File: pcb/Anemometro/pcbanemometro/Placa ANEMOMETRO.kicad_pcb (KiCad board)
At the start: 2 copper layers, 35.2 x 30 mm, 14 parts, among them J1 Conn_01x03, J2 Conn_01x03, U1 TL082

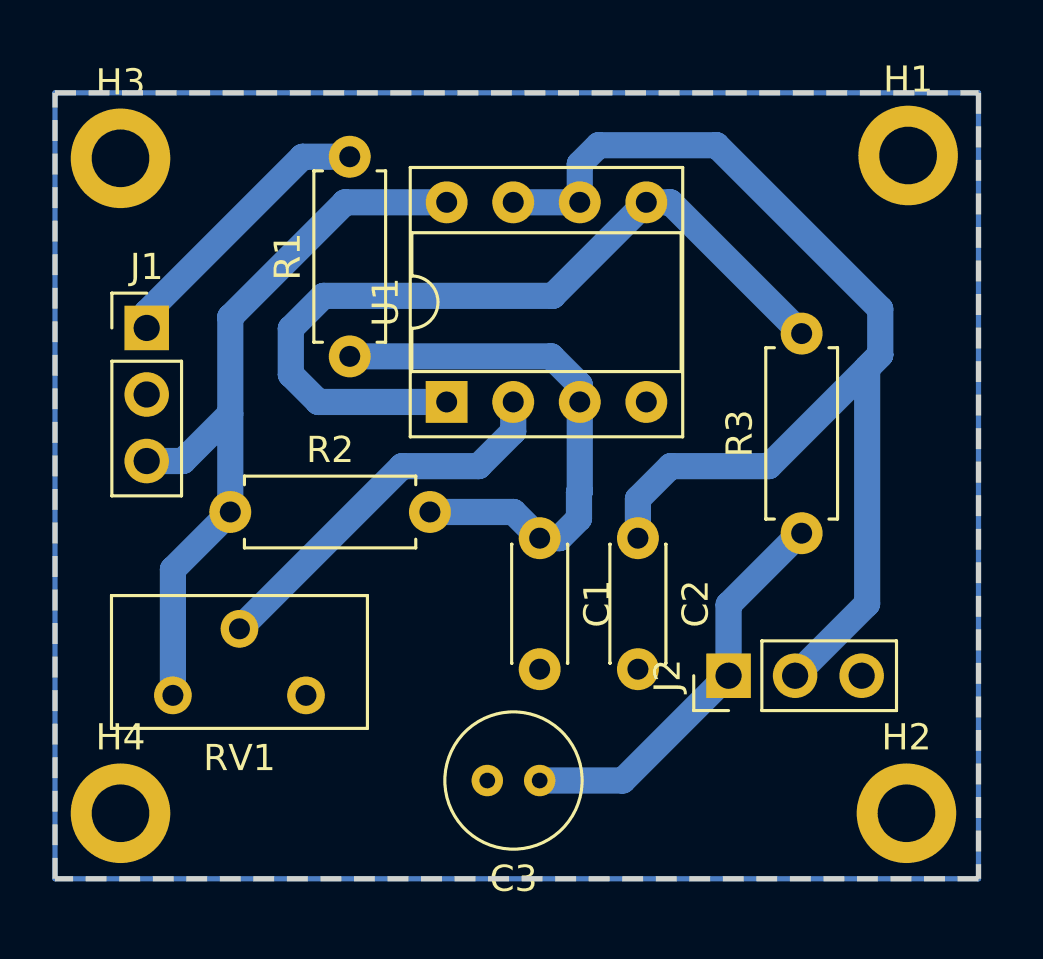
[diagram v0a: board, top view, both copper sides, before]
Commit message: se readaptaron y revisaron las PCBs, listas para imprimir
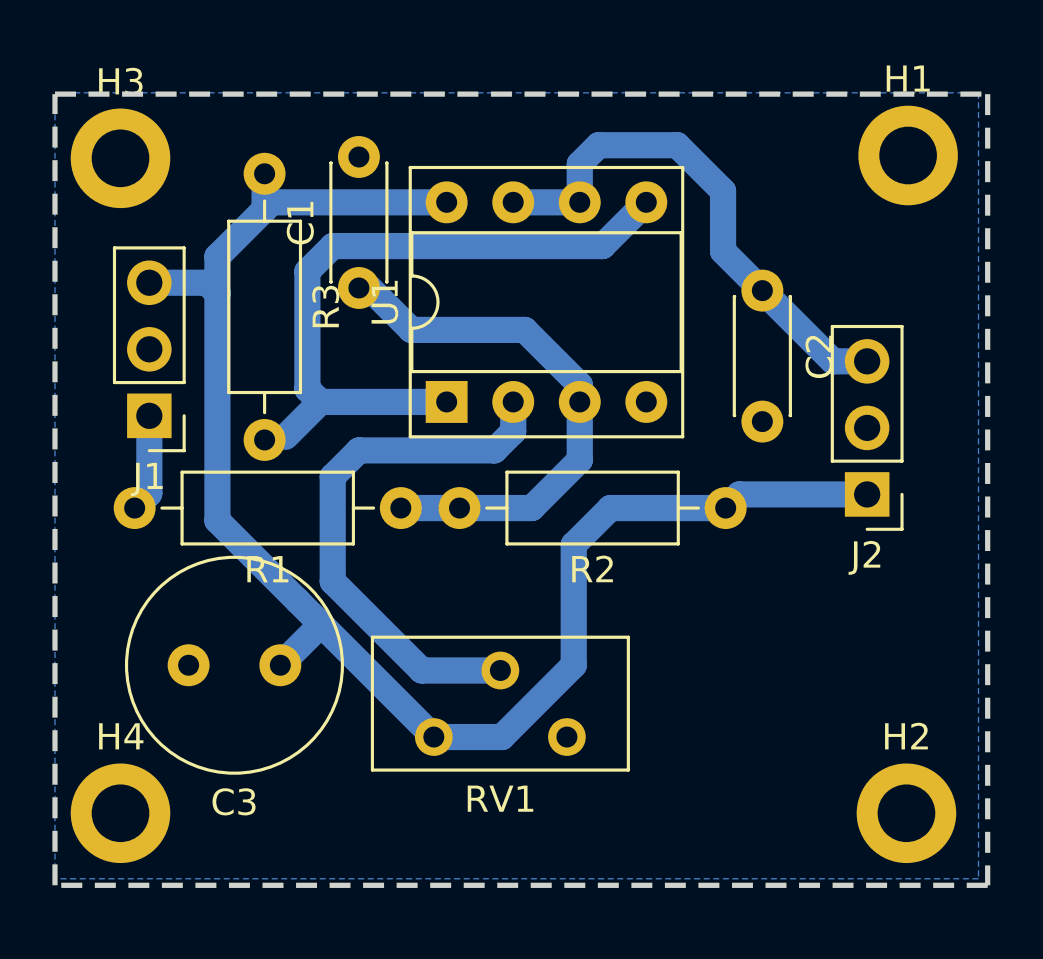
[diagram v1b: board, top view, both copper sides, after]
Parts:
- C3: footprint Capacitor_THT:C_Radial_D5.0mm_H7.0mm_P2.00mm -> Capacitor_THT:C_Radial_D8.0mm_H7.0mm_P3.50mm
- J2: value Conn_01x03 -> ToMother
- R1, R2, R3: footprint Resistor_THT:R_Axial_DIN0207_L6.3mm_D2.5mm_P7.62mm_Horizontal -> Resistor_THT:R_Axial_DIN0207_L6.3mm_D2.5mm_P10.16mm_Horizontal
- moved R3 24.7 mm to (83.0, 27.8), turned to -90 degrees
- moved R2 18.9 mm to (100.6, 40.6), turned to 180 degrees
- moved C1 11.8 mm to (86.6, 32.2), turned to 90 degrees
- moved C3 10.8 mm to (83.6, 46.6)
- moved C2 10.6 mm to (102.0, 32.3)
- moved RV1 10.1 mm to (89.5, 49.3)
- moved J2 8.71 mm to (106.0, 40.1), turned to 180 degrees
- moved R1 6.11 mm to (88.2, 40.6), turned to 180 degrees
- moved J1 3.36 mm to (78.6, 37.1), turned to 180 degrees
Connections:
- J2 pad 2: D_hall -> GND_G1
- J2 pad 3: GND_G1 -> D_hall
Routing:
- net D_hall: track 46.7 -> 20.0 mm
- net 3.3V: track 44.9 -> 60.8 mm
- net Net-(J1-Pin_1): track 10.8 -> 3.75 mm
- net Net-(U1A--): track 14.7 -> 20.5 mm
- net Net-(U1B-+): track 31.8 -> 26.0 mm
- net Net-(U1A-+): track 20.8 -> 20.0 mm
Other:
- board size 35.2 x 30 mm -> 35.6 x 30.2 mm

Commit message: Se agregó la modificación del MQ135 a 5v con divisor resistivo; además de cambio del DHT del pin 12; también se modificaron los pines de conexión
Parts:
- added C1: 104, Capacitor_THT:C_Disc_D4.3mm_W1.9mm_P5.00mm, F.Cu at (151.4, 121.8)
- added C1: 104, Capacitor_THT:C_Disc_D4.3mm_W1.9mm_P5.00mm, F.Cu at (205.2, 120.8)
- added C1: 104, Capacitor_THT:C_Disc_D4.3mm_W1.9mm_P5.00mm, F.Cu at (96.2, 123.0)
- added C1: 104, Capacitor_THT:C_Disc_D4.3mm_W1.9mm_P5.00mm, F.Cu at (205.4, 76.2)
- added C1: 104, Capacitor_THT:C_Disc_D4.3mm_W1.9mm_P5.00mm, F.Cu at (152.0, 77.4)
- added C2: 104, Capacitor_THT:C_Disc_D4.3mm_W1.9mm_P5.00mm, F.Cu at (220.6, 120.9)
- added C2: 104, Capacitor_THT:C_Disc_D4.3mm_W1.9mm_P5.00mm, F.Cu at (167.4, 77.5)
- added C2: 104, Capacitor_THT:C_Disc_D4.3mm_W1.9mm_P5.00mm, F.Cu at (111.6, 123.2)
- added C2: 104, Capacitor_THT:C_Disc_D4.3mm_W1.9mm_P5.00mm, F.Cu at (166.8, 121.9)
- added C2: 104, Capacitor_THT:C_Disc_D4.3mm_W1.9mm_P5.00mm, F.Cu at (220.8, 76.3)
- added C3: 220uF, Capacitor_THT:C_Radial_D8.0mm_H7.0mm_P3.50mm, F.Cu at (93.2, 137.4)
- added C3: 220uF, Capacitor_THT:C_Radial_D8.0mm_H7.0mm_P3.50mm, F.Cu at (202.4, 90.6)
- added C3: 220uF, Capacitor_THT:C_Radial_D8.0mm_H7.0mm_P3.50mm, F.Cu at (148.4, 136.2)
- added C3: 220uF, Capacitor_THT:C_Radial_D8.0mm_H7.0mm_P3.50mm, F.Cu at (149.0, 91.8)
- added C3: 220uF, Capacitor_THT:C_Radial_D8.0mm_H7.0mm_P3.50mm, F.Cu at (202.2, 135.2)
- added H1: MountingHole_Pad, MountingHole:MountingHole_2.2mm_M2_DIN965_Pad, F.Cu at (226.2, 115.7)
- added H1: MountingHole_Pad, MountingHole:MountingHole_2.2mm_M2_DIN965_Pad, F.Cu at (172.4, 116.7)
- added H1: MountingHole_Pad, MountingHole:MountingHole_2.2mm_M2_DIN965_Pad, F.Cu at (117.2, 118.0)
- added H1: MountingHole_Pad, MountingHole:MountingHole_2.2mm_M2_DIN965_Pad, F.Cu at (226.4, 71.1)
- added H1: MountingHole_Pad, MountingHole:MountingHole_2.2mm_M2_DIN965_Pad, F.Cu at (173.0, 72.3)
- added H2: MountingHole_Pad, MountingHole:MountingHole_2.2mm_M2_DIN965_Pad, F.Cu at (117.1, 143.1)
- added H2: MountingHole_Pad, MountingHole:MountingHole_2.2mm_M2_DIN965_Pad, F.Cu at (172.3, 141.8)
- added H2: MountingHole_Pad, MountingHole:MountingHole_2.2mm_M2_DIN965_Pad, F.Cu at (226.3, 96.2)
- added H2: MountingHole_Pad, MountingHole:MountingHole_2.2mm_M2_DIN965_Pad, F.Cu at (226.1, 140.8)
- added H2: MountingHole_Pad, MountingHole:MountingHole_2.2mm_M2_DIN965_Pad, F.Cu at (172.9, 97.5)
- added H3: MountingHole_Pad, MountingHole:MountingHole_2.2mm_M2_DIN965_Pad, F.Cu at (196.1, 115.8)
- added H3: MountingHole_Pad, MountingHole:MountingHole_2.2mm_M2_DIN965_Pad, F.Cu at (196.3, 71.2)
- added H3: MountingHole_Pad, MountingHole:MountingHole_2.2mm_M2_DIN965_Pad, F.Cu at (142.3, 116.8)
- added H3: MountingHole_Pad, MountingHole:MountingHole_2.2mm_M2_DIN965_Pad, F.Cu at (142.9, 72.5)
- added H3: MountingHole_Pad, MountingHole:MountingHole_2.2mm_M2_DIN965_Pad, F.Cu at (87.1, 118.1)
- added H4: MountingHole_Pad, MountingHole:MountingHole_2.2mm_M2_DIN965_Pad, F.Cu at (196.3, 96.2)
- added H4: MountingHole_Pad, MountingHole:MountingHole_2.2mm_M2_DIN965_Pad, F.Cu at (142.3, 141.8)
- added H4: MountingHole_Pad, MountingHole:MountingHole_2.2mm_M2_DIN965_Pad, F.Cu at (87.1, 143.1)
- added H4: MountingHole_Pad, MountingHole:MountingHole_2.2mm_M2_DIN965_Pad, F.Cu at (196.1, 140.8)
- added H4: MountingHole_Pad, MountingHole:MountingHole_2.2mm_M2_DIN965_Pad, F.Cu at (142.9, 97.5)
- added J1: Conn_01x03, Connector_PinHeader_2.54mm:PinHeader_1x03_P2.54mm_Vertical, F.Cu at (144.0, 82.3)
- added J1: Conn_01x03, Connector_PinHeader_2.54mm:PinHeader_1x03_P2.54mm_Vertical, F.Cu at (197.4, 81.1)
- added J1: Conn_01x03, Connector_PinHeader_2.54mm:PinHeader_1x03_P2.54mm_Vertical, F.Cu at (88.2, 127.9)
- added J1: Conn_01x03, Connector_PinHeader_2.54mm:PinHeader_1x03_P2.54mm_Vertical, F.Cu at (197.2, 125.7)
- added J1: Conn_01x03, Connector_PinHeader_2.54mm:PinHeader_1x03_P2.54mm_Vertical, F.Cu at (143.4, 126.7)
- added J2: ToMother, Connector_PinHeader_2.54mm:PinHeader_1x03_P2.54mm_Vertical, F.Cu at (224.6, 128.7)
- added J2: ToMother, Connector_PinHeader_2.54mm:PinHeader_1x03_P2.54mm_Vertical, F.Cu at (170.8, 129.7)
- added J2: ToMother, Connector_PinHeader_2.54mm:PinHeader_1x03_P2.54mm_Vertical, F.Cu at (171.4, 85.3)
- added J2: ToMother, Connector_PinHeader_2.54mm:PinHeader_1x03_P2.54mm_Vertical, F.Cu at (224.8, 84.1)
- added J2: ToMother, Connector_PinHeader_2.54mm:PinHeader_1x03_P2.54mm_Vertical, F.Cu at (115.6, 130.9)
- added R1: 100, Resistor_THT:R_Axial_DIN0207_L6.3mm_D2.5mm_P10.16mm_Horizontal, F.Cu at (153.6, 85.8)
- added R1: 100, Resistor_THT:R_Axial_DIN0207_L6.3mm_D2.5mm_P10.16mm_Horizontal, F.Cu at (207.0, 84.6)
- added R1: 100, Resistor_THT:R_Axial_DIN0207_L6.3mm_D2.5mm_P10.16mm_Horizontal, F.Cu at (97.8, 131.4)
- added R1: 100, Resistor_THT:R_Axial_DIN0207_L6.3mm_D2.5mm_P10.16mm_Horizontal, F.Cu at (206.8, 129.2)
- added R1: 100, Resistor_THT:R_Axial_DIN0207_L6.3mm_D2.5mm_P10.16mm_Horizontal, F.Cu at (153.0, 130.2)
- added R2: 1k, Resistor_THT:R_Axial_DIN0207_L6.3mm_D2.5mm_P10.16mm_Horizontal, F.Cu at (219.4, 84.6)
- added R2: 1k, Resistor_THT:R_Axial_DIN0207_L6.3mm_D2.5mm_P10.16mm_Horizontal, F.Cu at (165.4, 130.2)
- added R2: 1k, Resistor_THT:R_Axial_DIN0207_L6.3mm_D2.5mm_P10.16mm_Horizontal, F.Cu at (219.2, 129.2)
- added R2: 1k, Resistor_THT:R_Axial_DIN0207_L6.3mm_D2.5mm_P10.16mm_Horizontal, F.Cu at (166.0, 85.8)
- added R2: 1k, Resistor_THT:R_Axial_DIN0207_L6.3mm_D2.5mm_P10.16mm_Horizontal, F.Cu at (110.2, 131.4)
- added R3: 10k, Resistor_THT:R_Axial_DIN0207_L6.3mm_D2.5mm_P10.16mm_Horizontal, F.Cu at (147.8, 117.4)
- added R3: 10k, Resistor_THT:R_Axial_DIN0207_L6.3mm_D2.5mm_P10.16mm_Horizontal, F.Cu at (201.8, 71.8)
- added R3: 10k, Resistor_THT:R_Axial_DIN0207_L6.3mm_D2.5mm_P10.16mm_Horizontal, F.Cu at (92.6, 118.7)
- added R3: 10k, Resistor_THT:R_Axial_DIN0207_L6.3mm_D2.5mm_P10.16mm_Horizontal, F.Cu at (148.4, 73.0)
- added R3: 10k, Resistor_THT:R_Axial_DIN0207_L6.3mm_D2.5mm_P10.16mm_Horizontal, F.Cu at (201.6, 116.4)
- added RV1: 100k, Potentiometer_THT:Potentiometer_Bourns_3296Y_Vertical, F.Cu at (99.1, 140.2)
- added RV1: 100k, Potentiometer_THT:Potentiometer_Bourns_3296Y_Vertical, F.Cu at (154.9, 94.5)
- added RV1: 100k, Potentiometer_THT:Potentiometer_Bourns_3296Y_Vertical, F.Cu at (154.3, 138.9)
- added RV1: 100k, Potentiometer_THT:Potentiometer_Bourns_3296Y_Vertical, F.Cu at (208.1, 137.9)
- added RV1: 100k, Potentiometer_THT:Potentiometer_Bourns_3296Y_Vertical, F.Cu at (208.3, 93.3)
- added U1: TL082, Package_DIP:DIP-8_W7.62mm_Socket, F.Cu at (154.8, 126.2)
- added U1: TL082, Package_DIP:DIP-8_W7.62mm_Socket, F.Cu at (99.5, 127.4)
- added U1: TL082, Package_DIP:DIP-8_W7.62mm_Socket, F.Cu at (155.3, 81.8)
- added U1: TL082, Package_DIP:DIP-8_W7.62mm_Socket, F.Cu at (208.6, 125.2)
- added U1: TL082, Package_DIP:DIP-8_W7.62mm_Socket, F.Cu at (208.8, 80.5)
- moved C2 47.1 mm to (112.8, 78.2)
- moved J1 47.1 mm to (89.4, 82.9)
- moved J2 47.1 mm to (116.8, 85.9)
- moved U1 47.1 mm to (100.8, 82.4)
- moved C1 47.1 mm to (97.4, 78.0)
- moved C3 47.1 mm to (94.4, 92.5)
- moved R1 47.1 mm to (99.0, 86.5)
- moved R2 47.1 mm to (111.4, 86.5)
- moved RV1 47.1 mm to (100.3, 95.2)
- moved H1 47.1 mm to (118.4, 73.0)
- moved H2 47.1 mm to (118.3, 98.1)
- moved H3 47.1 mm to (88.3, 73.1)
- moved H4 47.1 mm to (88.3, 98.1)
- moved R3 47.1 mm to (93.8, 73.7)
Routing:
- net 3.3V: track 60.8 -> 364.6 mm
- net Net-(U1B-+): track 26.0 -> 155.9 mm
- net Net-(U1A--): track 20.5 -> 123.2 mm
- net D_hall: track 20.0 -> 120.2 mm
- net Net-(U1A-+): track 20.0 -> 120.1 mm
- net Net-(J1-Pin_1): track 3.75 -> 22.5 mm
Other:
- board size 35.6 x 30.2 mm -> 144.8 x 77 mm
- board text added: "Anemó v:1.0"
